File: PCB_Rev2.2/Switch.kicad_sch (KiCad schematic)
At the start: 16 parts, among them SW10 SW_Push, SW2 RotaryEncoder_Switch_MP, SW3 RotaryEncoder_Switch_MP, SW4 SW_Push, SW5 SW_Push, SW6 SW_Push, SW7 SW_Push, SW8 SW_Push, SW9 SW_Push

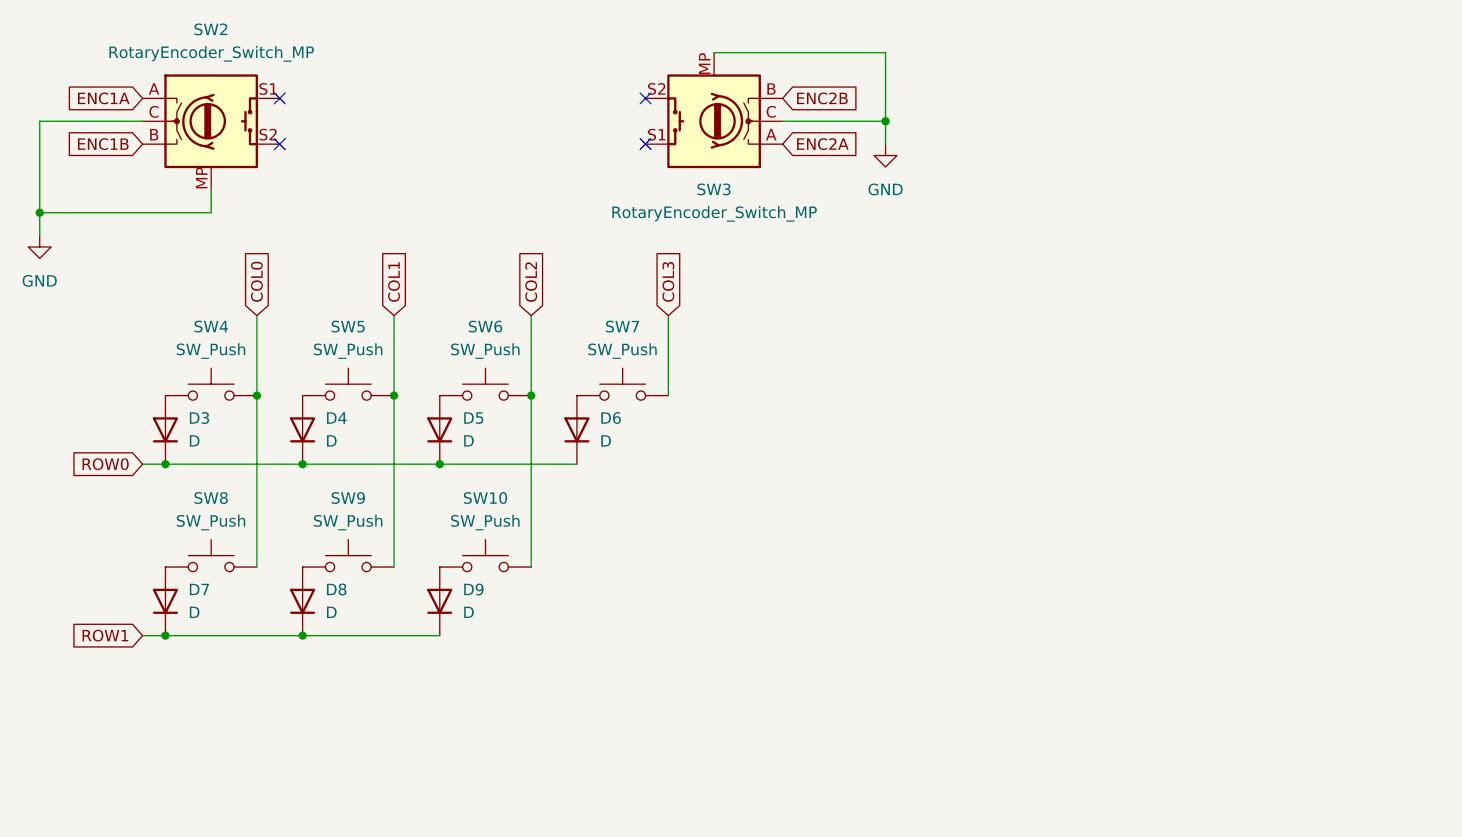
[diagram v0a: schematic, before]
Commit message: Before merge & open source.
Co-Authored-By: MAltmann <57740314+maltmannx@users.noreply.github.com>
Co-Authored-By: nonameCCC <79012391+nonameCCC@users.noreply.github.com>
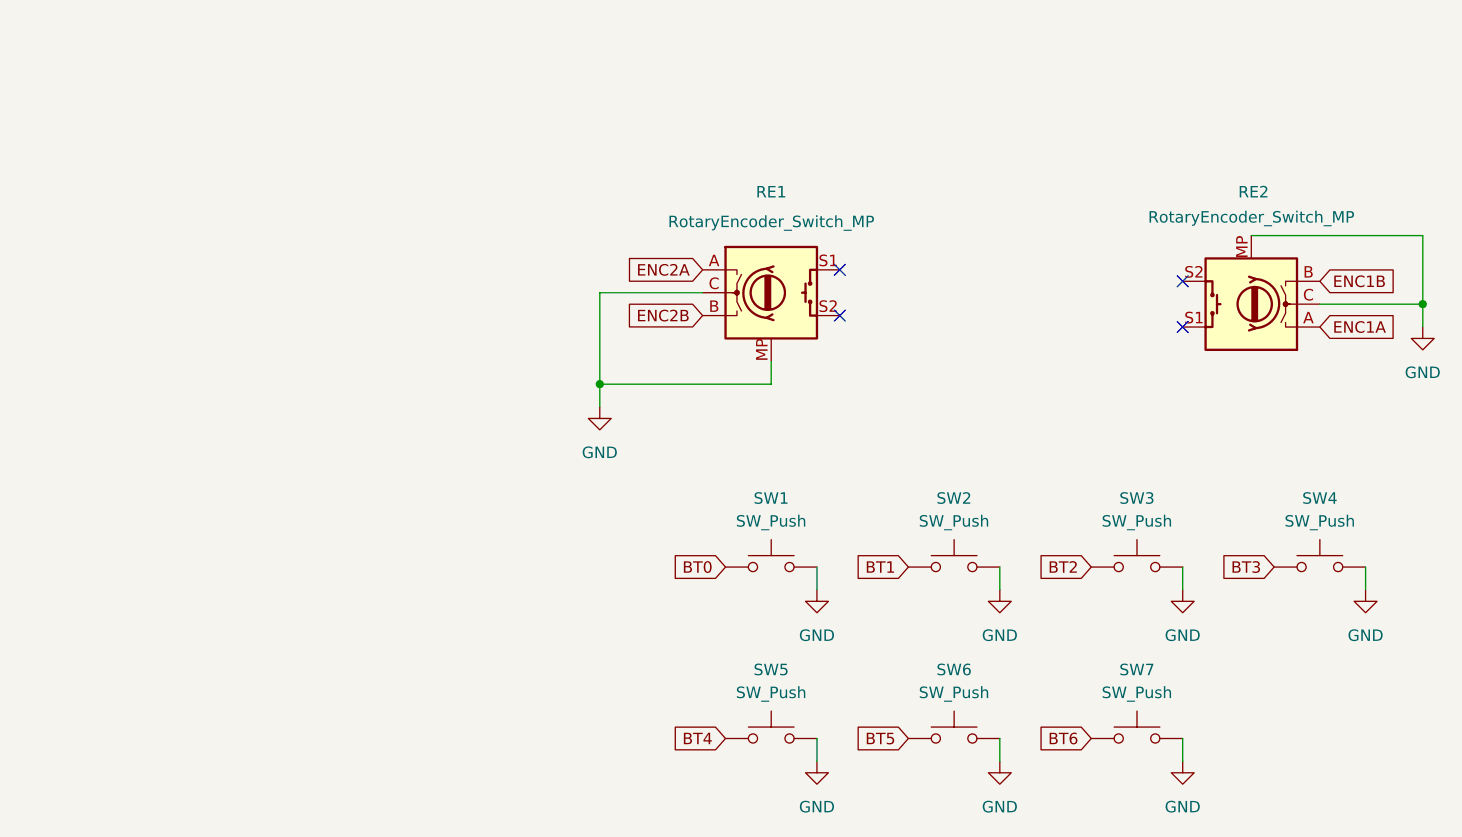
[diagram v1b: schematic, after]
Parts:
- removed D3, D4, D5, D6, D7, D8, D9: D, Diode_SMD:D_0402_1005Metric, symbol Device:D
- SW5: renamed from SW8; footprint PCM_Switch_Keyboard_Hotswap_Kailh:SW_Hotswap_Kailh_MX_2.75u -> PCM_Switch_Keyboard_Hotswap_Kailh:SW_Hotswap_Kailh_MX_2.25u
- SW7: renamed from SW10; footprint PCM_Switch_Keyboard_Hotswap_Kailh:SW_Hotswap_Kailh_MX_2.75u -> PCM_Switch_Keyboard_Hotswap_Kailh:SW_Hotswap_Kailh_MX_2.25u
- renumbered SW2 to RE1, SW3 to RE2, SW4 to SW1, SW5 to SW2, SW6 to SW3, SW7 to SW4, SW9 to SW6
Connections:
- net COL0 is gone; now on net GND: SW1.2, SW5.2
- net COL1 is gone; now on net GND: SW2.2, SW6.2
- net COL2 is gone; now on net GND: SW3.2, SW7.2
- net COL3 is gone; now on net GND: SW4.2
- net ENC1A: now also RE2.A; no longer RE1.A
- net ENC1B: now also RE2.B; no longer RE1.B
- net ENC2A: now also RE1.A; no longer RE2.A
- net ENC2B: now also RE1.B; no longer RE2.B
- net BT0: now reaches SW1.1
- net BT1: now reaches SW2.1
- net BT4: now reaches SW5.1
- net BT6: now reaches SW7.1
- net BT2: now reaches SW3.1
- net BT3: now reaches SW4.1
- net BT5: now reaches SW6.1
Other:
- company: (none) -> Team PHDesign
- title: (none) -> PH-AC  --Another controller for Genshin-impact-like game.
- moved on the sheet: RE1, RE2, SW1, SW2, SW3, SW4, SW5, SW6, SW7
